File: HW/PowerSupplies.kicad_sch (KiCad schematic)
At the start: 16 parts, among them U3 LR7533-T, U4 LM317EMPX/NOPB

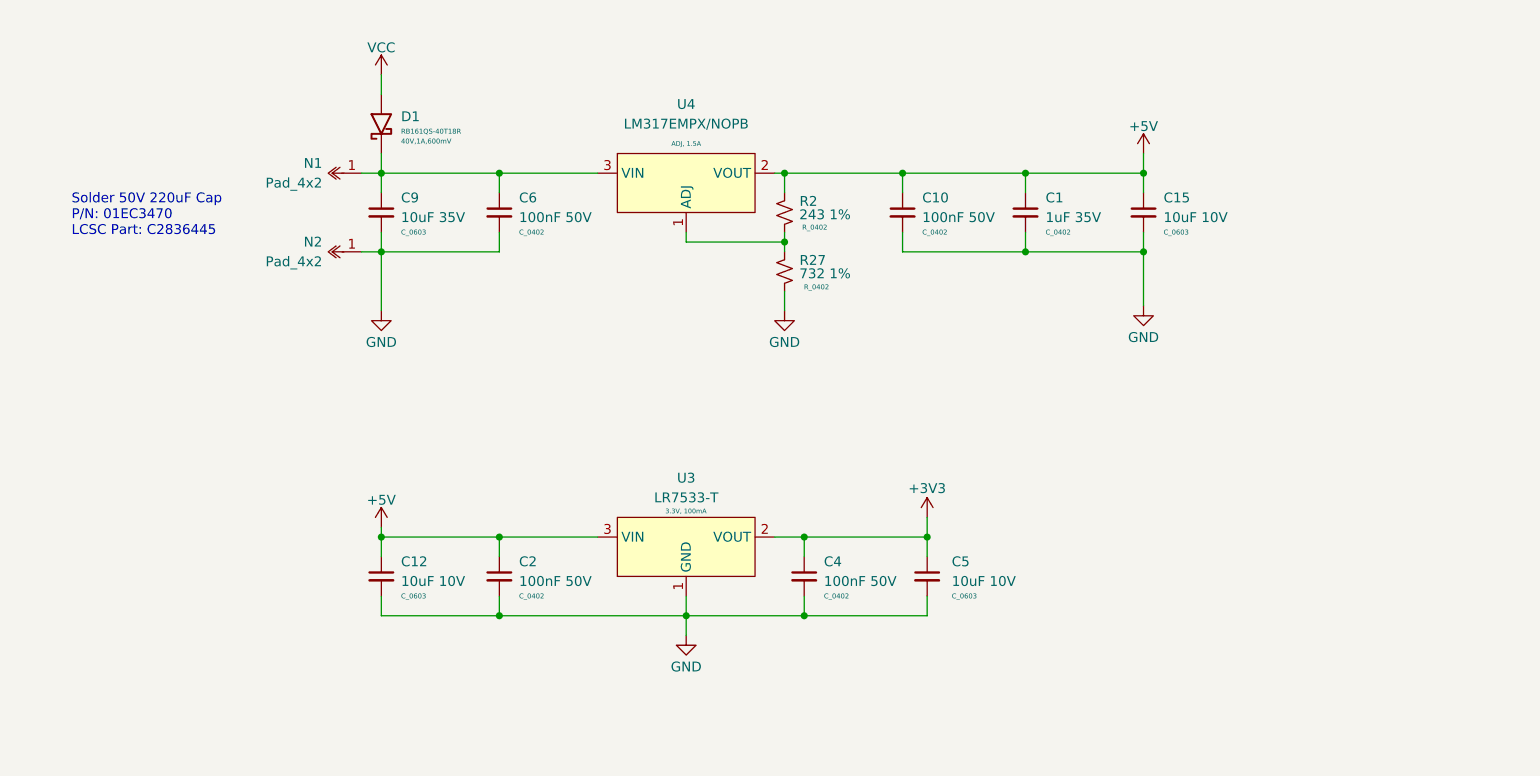
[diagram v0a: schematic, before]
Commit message: WIP - Layout XT30/PCB Finger Positions
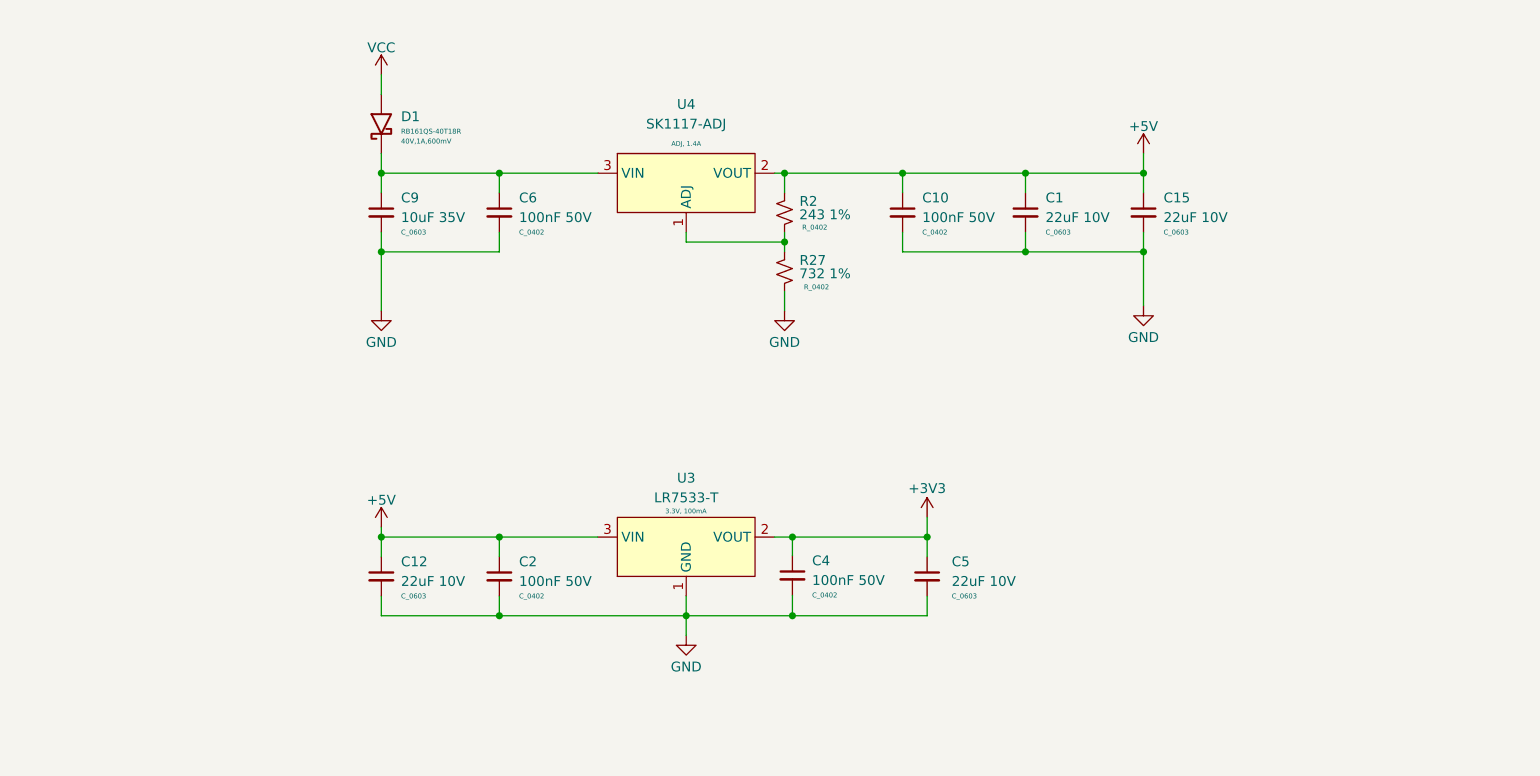
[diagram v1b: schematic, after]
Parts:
- removed C1: 1uF 35V, C_Capacitor:C_0402, symbol C_Capacitor:C_0402
- removed N1, N2: Pad_4x2, N_NonPart:Pad_4x2, symbol N_NonPart:Pad_4x2
- added C1: 22uF 10V, C_Capacitor:C_0603, symbol C_Capacitor:C_0603
- C12, C15, C5: value 10uF 10V -> 22uF 10V; LCSC Part C19702 -> C86295
- U4: value LM317EMPX/NOPB -> SK1117-ADJ; LCSC Part C352843 -> C475601; Params ADJ, 1.5A -> ADJ, 1.4A
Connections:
- net +5V: now also C1.1
- net GND: now also C1.2
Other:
- note removed: "Solder 50V 220uF Cap P/N: 01EC3470 LCSC Part: C2836445"
- title: WEKA ESC - 20A -> KAKAPO ESC - 20A

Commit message: WIP - Layout Motor Drivers + Buck Circuit
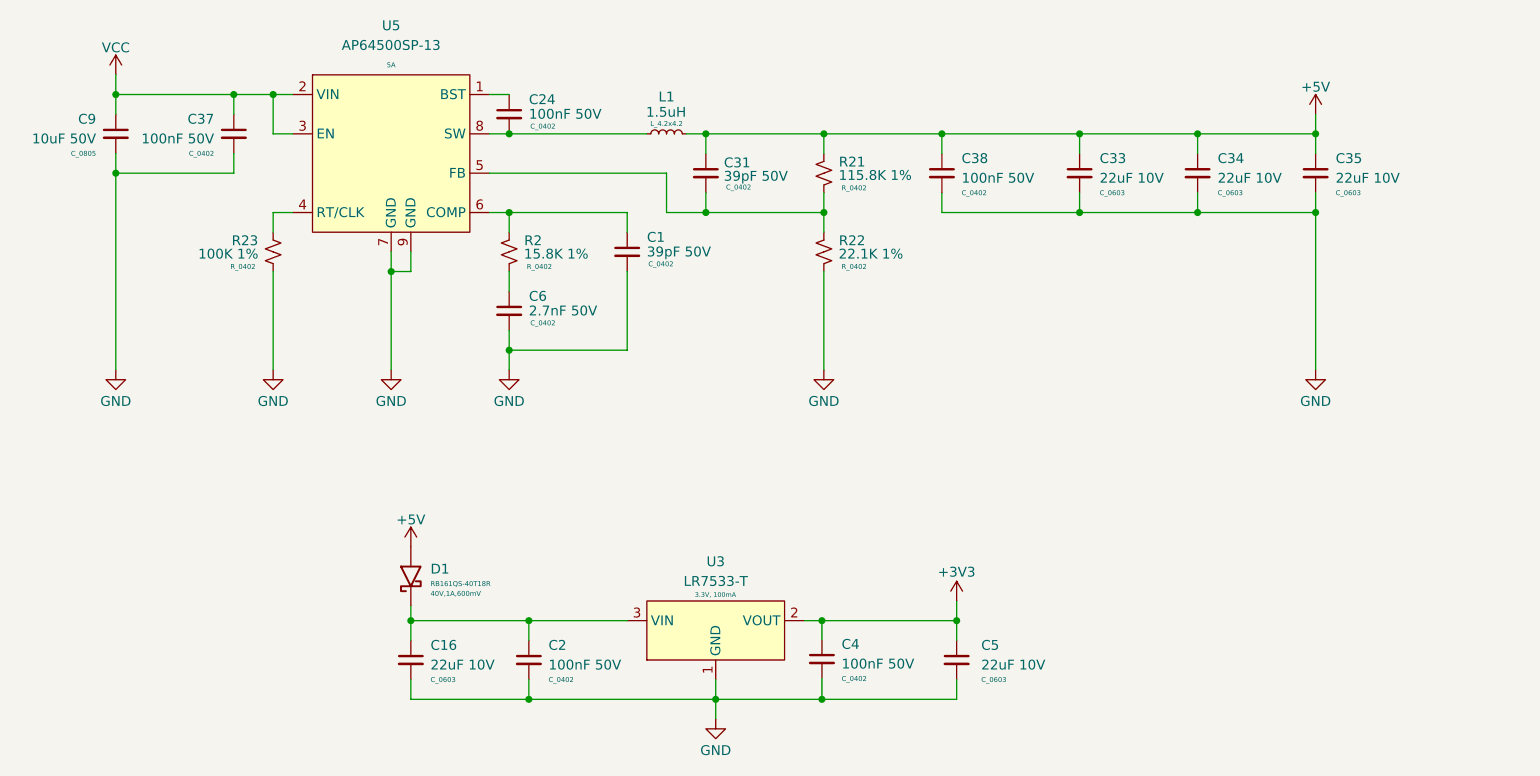
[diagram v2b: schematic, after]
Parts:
- removed C1, C12, C15: 22uF 10V, C_Capacitor:C_0603, symbol C_Capacitor:C_0603
- removed C10: 100nF 50V, C_Capacitor:C_0402, symbol C_Capacitor:C_0402
- removed C9: 10uF 35V, C_Capacitor:C_0603, symbol C_Capacitor:C_0603
- removed R27: 732 1%, R_Resistor:R_0402, symbol R_Resistor:R_0402
- removed U4: SK1117-ADJ, U_IC:SOT223_3, symbol U_Power:LM317EMPX/NOPB
- added C1, C31: 39pF 50V, C_Capacitor:C_0402, symbol C_Capacitor:C_0402
- added C16, C33, C34, C35: 22uF 10V, C_Capacitor:C_0603, symbol C_Capacitor:C_0603
- added C24, C37, C38: 100nF 50V, C_Capacitor:C_0402, symbol C_Capacitor:C_0402
- added C9: 10uF 50V, C_Capacitor:C_0805, symbol C_Capacitor:C_0805
- added L1: 1.5uH, L_Inductor:L_4.2x4.2, symbol L_Inductor:L_4.2x4.2
- added R21: 115.8K 1%, R_Resistor:R_0402, symbol R_Resistor:R_0402
- added R22: 22.1K 1%, R_Resistor:R_0402, symbol R_Resistor:R_0402
- added R23: 100K 1%, R_Resistor:R_0402, symbol R_Resistor:R_0402
- added U5: AP64500SP-13, U_IC:SOIC_8_EP, symbol U_Power:AP64500SP-13
- C6: value 100nF 50V -> 2.7nF 50V; LCSC Part C105882 -> (none)
- R2: value 243 1% -> 15.8K 1%; LCSC Part C226367 -> (none)
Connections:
- net +5V: now also D1.2, C31.1, C33.1, C34.1, C35.1, C38.1, L1.2, R21.1; no longer C2.1, R2.1, U3.3 (VIN)
- net GND: now also C1.2, C16.2, C33.2, C34.2, C35.2, C37.2, C38.2, C9.2, R22.2, R23.2, U5.7 (GND), U5.9 (GND)
- net VCC: now also C37.1, C9.1, U5.2 (VIN), U5.3 (EN); no longer D1.2
- net at D1.1: now also C2.1, U3.3 (VIN), C16.1; no longer C6.1
- net at R2.2: now also C6.1
- new net: R23.1, U5.4 (RT/CLK)
- new net: C24.1, U5.1 (BST)
- new net: C24.2, L1.1, U5.8 (SW)
- new net: C1.1, R2.1, U5.6 (COMP)
- new net: C31.2, R21.2, R22.1, U5.5 (FB)
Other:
- moved on the sheet: C2, C4, C5, U3

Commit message: Finish Tracking and Release For MFG
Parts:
- added C39: 22uF 10V, C_Capacitor:C_0603, symbol C_Capacitor:C_0603
- L1: LCSC Part (none) -> C2921165; LCSC_Part C2921165 -> (none); MFG Part (none) -> BCIHP0420SC-1R5M; MFG_Part BCIHP0420SC-1R5M -> (none)
- R2: LCSC Part (none) -> C26956
- R21: LCSC Part (none) -> C3013150
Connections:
- net +5V: now also C39.1
- net GND: now also C39.2
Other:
- title: KAKAPO ESC - 20A -> KAKAPO - 20A
- moved on the sheet: C35

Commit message: Update gitignore
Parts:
- R22: LCSC Part C226367 -> (none)
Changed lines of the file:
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@@
       (effects (font (size 0.635 0.635)))
     )
-    (property "LCSC Part" "C226367" (at 165.1 81.915 0)
+    (property "LCSC Part" "" (at 165.1 81.915 0)
       (effects (font (size 1.27 1.27)) hide)
     )

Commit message: Fix Motor Driver Comms Tracking Issue
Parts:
- R21: value 115.8K 1% -> 118K 1%; LCSC Part C3013150 -> (none)
- R22: value 22.1K 1% -> 22K 1%
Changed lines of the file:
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@@
       (effects (font (size 1.27 1.27)) (justify right))
     )
-    (property "Value" "22.1K 1%" (at 167.005 82.1943 0)
+    (property "Value" "22K 1%" (at 167.005 82.1943 0)
       (effects (font (size 1.27 1.27)) (justify right))
     )
@@
       (effects (font (size 1.27 1.27)) (justify right))
     )
-    (property "Value" "115.8K 1%" (at 167.005 72.0343 0)
+    (property "Value" "118K 1%" (at 167.005 72.0343 0)
       (effects (font (size 1.27 1.27)) (justify right))
     )
@@
       (effects (font (size 0.635 0.635)))
     )
-    (property "LCSC Part" "C3013150" (at 165.1 71.755 0)
-      (effects (font (size 1.27 1.27)) hide)
-    )
+    (property "LCSC Part" "" (at 165.1 71.755 0)
+      (effects (font (size 1.27 1.27)) hide)
+    )

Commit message: Create v1.0 Fixed From v0.2 HW
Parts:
- C1: LCSC Part C105882 -> C106223
- C31: LCSC Part (none) -> C106223
- C6: LCSC Part (none) -> C106251
- R21: LCSC Part (none) -> C5126219
- R22: LCSC Part (none) -> C2909337
- R23: LCSC Part (none) -> C60491
- U3: MFG Part (none) -> LR7533-T; MPN LR7533-T -> (none)
- U5: LCSC Part (none) -> C2070920
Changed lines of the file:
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@@
       (effects (font (size 0.635 0.635)))
     )
-    (property "LCSC Part" "" (at 93.98 81.915 0)
+    (property "LCSC Part" "C60491" (at 93.98 81.915 0)
       (effects (font (size 1.27 1.27)) hide)
     )
@@
       (effects (font (size 0.635 0.635)) (justify left))
     )
-    (property "LCSC Part" "" (at 124.46 89.535 0)
+    (property "LCSC Part" "C106251" (at 124.46 89.535 0)
       (effects (font (size 1.27 1.27)) hide)
     )
@@
       (effects (font (size 0.635 0.635)))
     )
-    (property "LCSC Part" "" (at 165.1 81.915 0)
+    (property "LCSC Part" "C2909337" (at 165.1 81.915 0)
       (effects (font (size 1.27 1.27)) hide)
     )
@@
     (property "Params" "5A" (at 109.22 57.785 0)
       (effects (font (size 0.63 0.63)))
+    )
+    (property "LCSC Part" "C2070920" (at 109.22 79.375 0)
+      (effects (font (size 1.27 1.27)) hide)
     )
     (pin "2")
@@
       (effects (font (size 0.635 0.635)) (justify left))
     )
-    (property "LCSC Part" "" (at 149.86 71.755 0)
+    (property "LCSC Part" "C106223" (at 149.86 71.755 0)
       (effects (font (size 1.27 1.27)) hide)
     )
@@
       (effects (font (size 0.635 0.635)))
     )
-    (property "LCSC Part" "" (at 165.1 71.755 0)
+    (property "LCSC Part" "C5126219" (at 165.1 71.755 0)
       (effects (font (size 1.27 1.27)) hide)
     )
@@
       (effects (font (size 0.6 0.6)))
     )
-    (property "MPN" "LR7533-T" (at 151.13 134.62 0)
+    (property "MFG Part" "LR7533-T" (at 151.13 134.62 0)
       (effects (font (size 1.27 1.27)) hide)
     )
@@
       (effects (font (size 0.635 0.635)) (justify left))
     )
-    (property "LCSC Part" "C105882" (at 139.7 81.915 0)
-      (effects (font (size 1.27 1.27)) hide)
-    )
+    (property "LCSC Part" "C106223" (at 139.7 81.915 0)
+      (effects (font (size 1.27 1.27)) hide)
+    )
